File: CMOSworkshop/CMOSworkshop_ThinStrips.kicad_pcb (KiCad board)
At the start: 2 copper layers, 160.5 x 65.6 mm, 64 parts, among them J1 JACK_STEREO, P1 CONN_01X03, P10 CONN_01X02, P11 CONN_01X03, P12 CONN_01X02, P13 CONN_01X03, P14 CONN_01X02, P15 CONN_01X03, P16 CONN_01X02, P17 CONN_01X02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

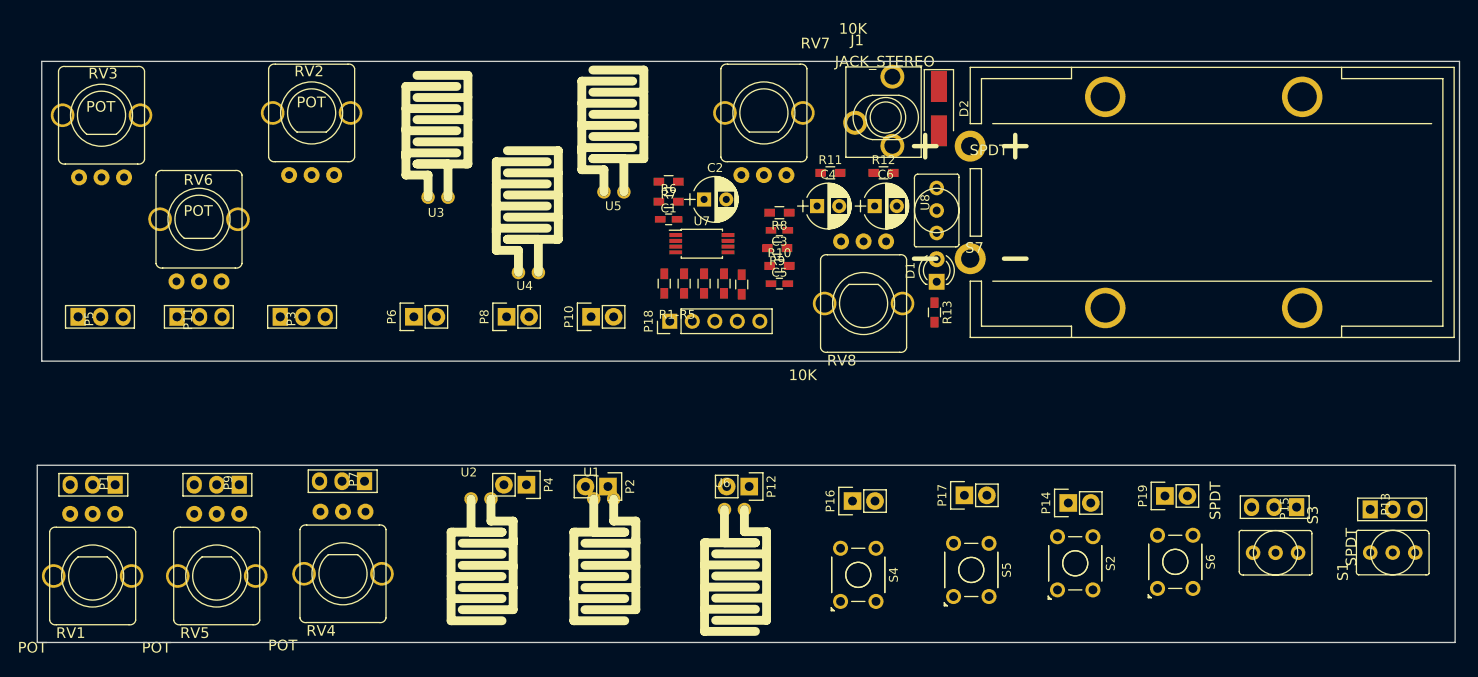
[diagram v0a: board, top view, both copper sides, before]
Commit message: updated mixer schematic, added 9v battery holder and laid out components.
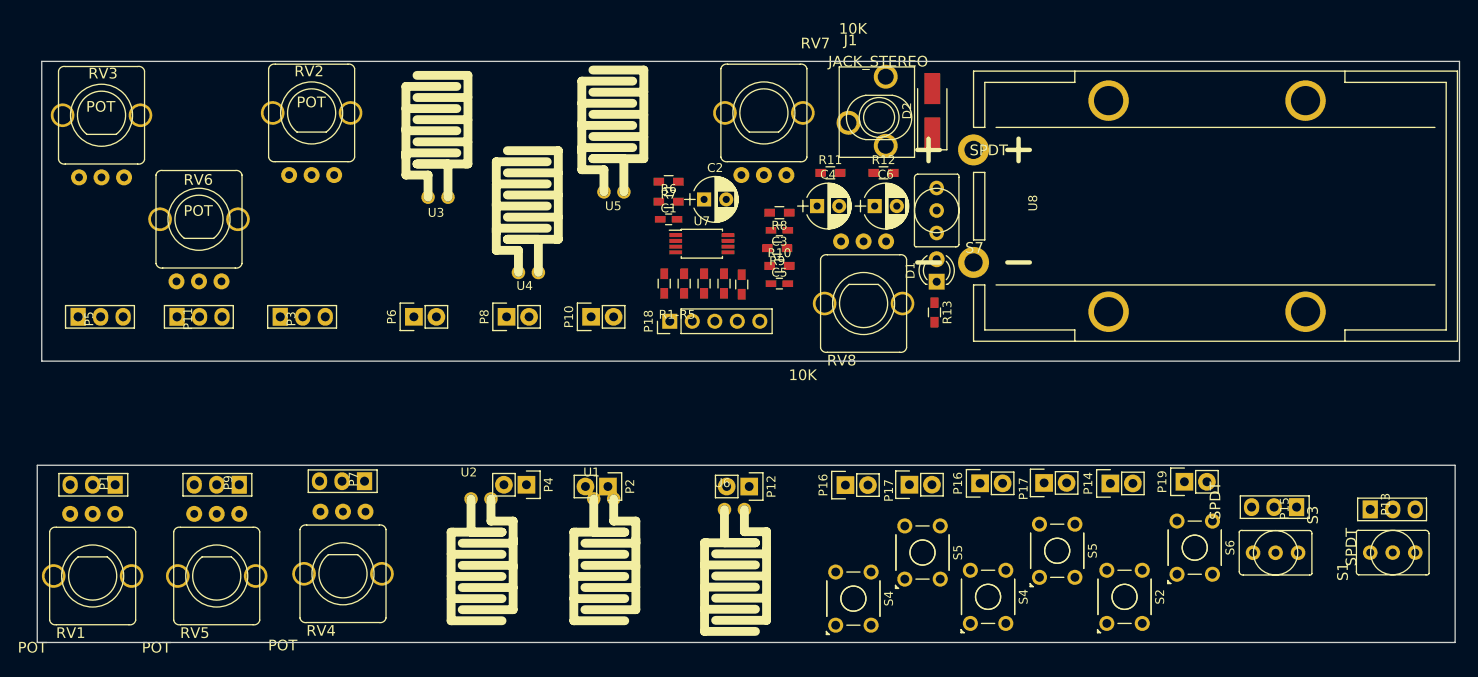
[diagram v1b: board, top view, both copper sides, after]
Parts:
- added P16: CONN_01X02, EtherkitKicadLibrary:Pin_Header_Straight_1x02, F.Cu at (190.7, 127.0)
- added P17: CONN_01X02, EtherkitKicadLibrary:Pin_Header_Straight_1x02, F.Cu at (197.9, 126.9)
- added S4: PUSHBUTTON_TACTILE, Buttons_Switches_ThroughHole:SW_TH_Tactile_Omron_B3F-10xx, F.Cu at (189.6, 142.8)
- added S5: PUSHBUTTON_TACTILE, Buttons_Switches_ThroughHole:SW_TH_Tactile_Omron_B3F-10xx, F.Cu at (197.4, 137.6)
- moved S4 14.9 mm to (204.8, 142.6)
- moved P16 14.5 mm to (205.9, 126.8)
- moved S5 9.93 mm to (212.6, 137.4)
- moved P17 9.11 mm to (213.1, 126.7)
- moved S2 6.73 mm to (220.2, 142.6)
- moved P14 5.24 mm to (220.6, 126.8)
- moved S6 2.72 mm to (228.1, 137.1)
- moved P19 2.72 mm to (229.0, 126.6)
- moved D2 0.79 mm to (200.5, 84.8), turned to 90 degrees
- moved J1 0.75 mm to (194.5, 85.5)
- moved U8 0.57 mm to (205.2, 89.2)

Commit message: added traces for mixer circuit and made small connection in hp mixer
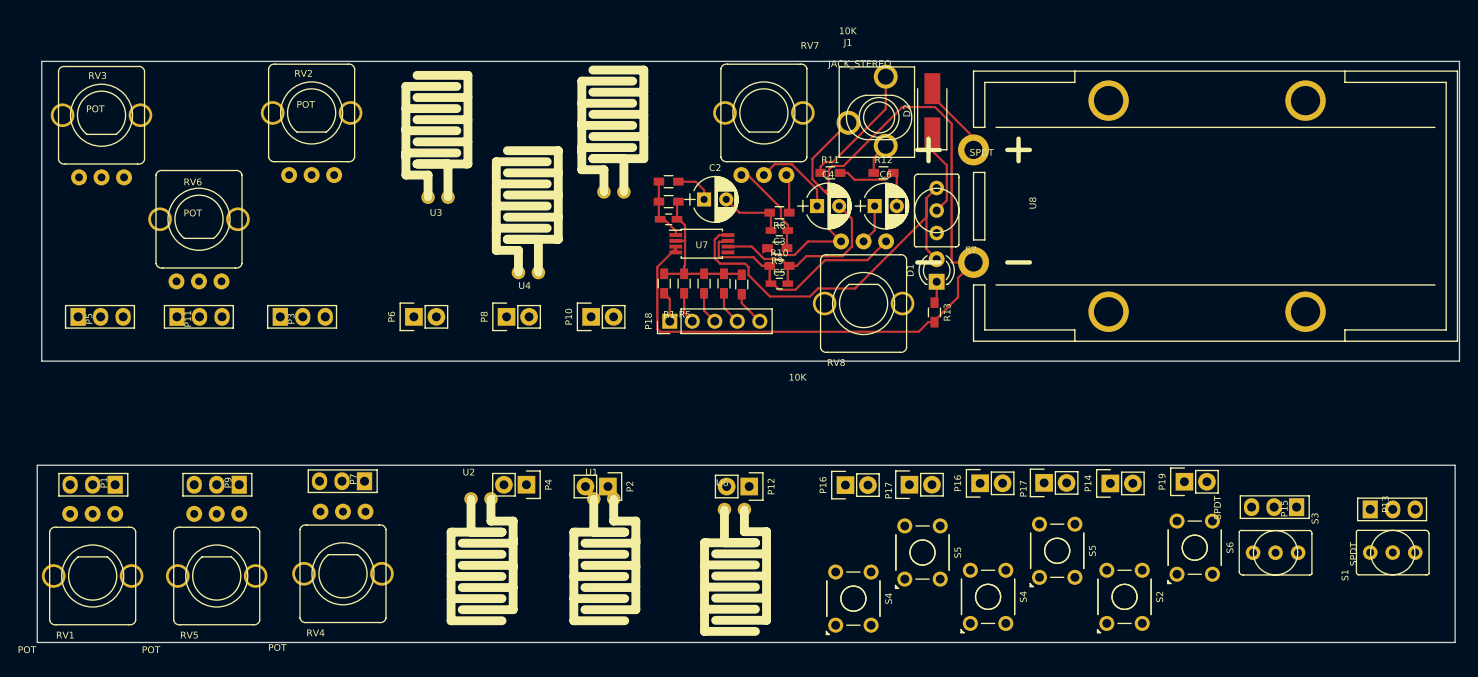
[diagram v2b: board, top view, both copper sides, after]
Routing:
- net GND: track 0.00 -> 115.7 mm
- net VCC: track 0.00 -> 44.9 mm
- net Net-(C5-Pad1): track 0.00 -> 26.5 mm
- net Net-(C4-Pad-): track 0.00 -> 23.0 mm
- net Net-(C1-Pad2): track 0.00 -> 18.6 mm
- net MIXOUTA: track 0.00 -> 14.4 mm
- net Net-(C3-Pad1): track 0.00 -> 10.9 mm
- net Net-(C6-Pad-): track 0.00 -> 10.6 mm
- net Net-(D2-Pad1): track 0.00 -> 9.91 mm
- net Net-(C4-Pad+): track 0.00 -> 9.55 mm
- net Net-(D2-Pad2): track 0.00 -> 8.84 mm
- net Net-(C2-Pad-): track 0.00 -> 7.58 mm
- net Net-(C1-Pad1): track 0.00 -> 7.08 mm
- net Net-(C6-Pad+): track 0.00 -> 4.51 mm
- net Net-(R8-Pad1): track 0.00 -> 4.38 mm
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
